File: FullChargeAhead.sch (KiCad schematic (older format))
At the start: 18 parts, among them CON101 USB-MICRO-B, P101 CONN_01X02, P102 JST 2 Pin, U101 MCP73834-FCI/UN

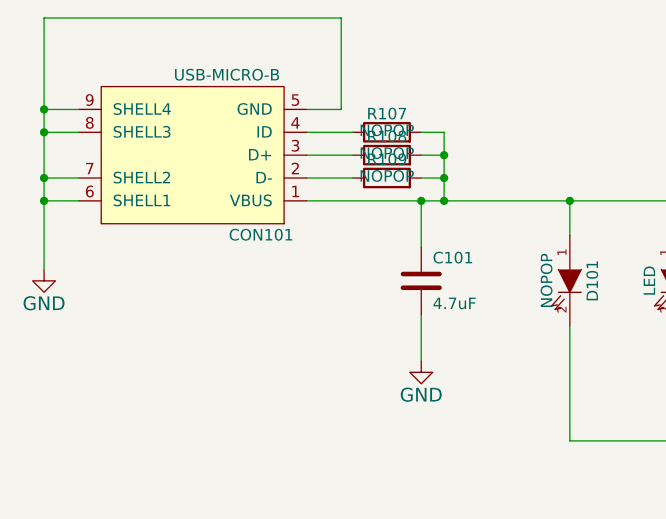
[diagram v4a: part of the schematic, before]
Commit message: Front Cu Layout done
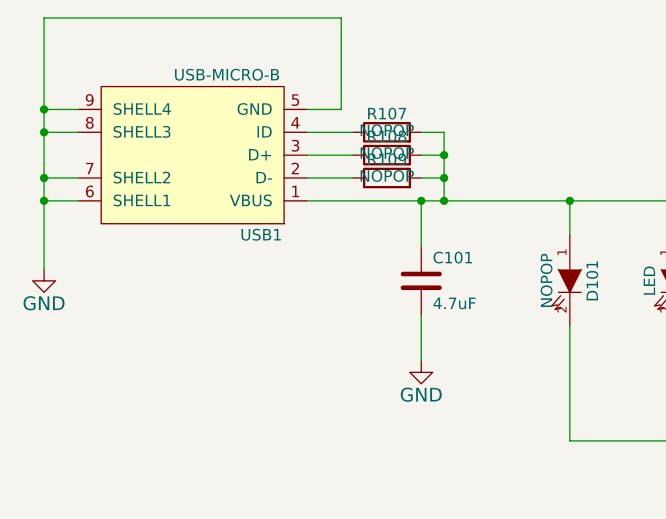
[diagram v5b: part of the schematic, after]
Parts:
- USB1: renamed from CON101; MPN (none) -> Value
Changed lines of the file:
@@
 	5500 4900 5500 5200
 $Comp
-L USB-MICRO-B CON101
+L USB-MICRO-B USB1
 U 1 1 550DCE37
 P 2700 2700
-F 0 "CON101" H 2400 3050 50  0000 C CNN
+F 0 "USB1" H 2400 3050 50  0000 C CNN
 F 1 "USB-MICRO-B" H 2550 2350 50  0000 C CNN
 F 2 "fca-lib:USB_Micro_B" H 2700 2600 50  0001 C CNN
 F 3 "" H 2700 2600 50  0000 C CNN
+F 4 "Value" H 2700 2700 60  0001 C CNN "MPN"
 	1    2700 2700
 	-1   0    0    1

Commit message: Started BOM
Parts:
- C101: ConradPN (none) -> 1278977 - 62
- C102: ConradPN (none) -> 1278977 - 62; MPN (none) -> Value
- D101: ConradPN (none) -> N/A; MPN (none) -> N/A
- D102, D103: ConradPN (none) -> 180102 - 62; MPN (none) -> KP-2012EC
- U101: ConradPN (none) -> 1085505 - 62; MPN (none) -> MCP73834-FCI/UN
- USB1: ConradPN (none) -> N/A; MPN Value -> 10118193-0001LF
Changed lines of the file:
@@
 F 2 "Housings_SSOP:MSOP-10_3x3mm_Pitch0.5mm" H 6700 3350 60  0001 C CNN
 F 3 "" H 6700 3350 60  0000 C CNN
+F 4 "MCP73834-FCI/UN" H 6900 3350 60  0001 C CNN "MPN"
+F 5 "1085505 - 62 " H 6900 3350 60  0001 C CNN "ConradPN"
 	1    6900 3350
 	1    0    0    -1
@@
 F 2 "LEDs:LED-0805" H 4350 3250 60  0001 C CNN
 F 3 "" H 4350 3250 60  0000 C CNN
+F 4 "N/A" H 4350 3250 60  0001 C CNN "MPN"
+F 5 "N/A" H 4350 3250 60  0001 C CNN "ConradPN"
 	1    4350 3250
 	0    1    1    0
@@
 F 2 "LEDs:LED-0805" H 4800 3250 60  0001 C CNN
 F 3 "" H 4800 3250 60  0000 C CNN
+F 4 "KP-2012EC" H 4800 3250 60  0001 C CNN "MPN"
+F 5 "180102 - 62" H 4800 3250 60  0001 C CNN "ConradPN"
 	1    4800 3250
 	0    1    1    0
@@
 F 2 "LEDs:LED-0805" H 5200 3250 60  0001 C CNN
 F 3 "" H 5200 3250 60  0000 C CNN
+F 4 "KP-2012EC" H 5200 3250 60  0001 C CNN "MPN"
+F 5 "180102 - 62" H 5200 3250 60  0001 C CNN "ConradPN"
 	1    5200 3250
 	0    1    1    0
@@
 F 3 "" H 3700 3250 60  0000 C CNN
 F 4 "Value" H 3700 3250 60  0001 C CNN "MPN"
+F 5 "1278977 - 62" H 3700 3250 60  0001 C CNN "ConradPN"
 	1    3700 3250
 	1    0    0    -1
@@
 F 2 "Capacitors_SMD:C_1206_HandSoldering" H 8938 3100 30  0001 C CNN
 F 3 "" H 8900 3250 60  0000 C CNN
+F 4 "Value" H 8900 3250 60  0001 C CNN "MPN"
+F 5 "1278977 - 62" H 8900 3250 60  0001 C CNN "ConradPN"
 	1    8900 3250
 	1    0    0    -1
@@
 F 2 "fca-lib:USB_Micro_B" H 2700 2600 50  0001 C CNN
 F 3 "" H 2700 2600 50  0000 C CNN
-F 4 "Value" H 2700 2700 60  0001 C CNN "MPN"
+F 4 "10118193-0001LF" H 2700 2700 60  0001 C CNN "MPN"
+F 5 "N/A" H 2700 2700 60  0001 C CNN "ConradPN"
 	1    2700 2700
 	-1   0    0    1

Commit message: Some changes and test results
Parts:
- R106: value 1K -> 2K
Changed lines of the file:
@@
 P 8050 3700
 F 0 "R106" V 8130 3700 50  0000 C CNN
-F 1 "1K" V 8057 3701 50  0000 C CNN
+F 1 "2K" V 8057 3701 50  0000 C CNN
 F 2 "Resistors_SMD:R_0805_HandSoldering" V 7980 3700 30  0001 C CNN
 F 3 "" H 8050 3700 30  0000 C CNN
@@
 U 1 1 55106F74
 P 3550 2700
-F 0 "R108" V 3630 2700 50  0000 C CNN
+F 0 "R108" V 3500 2900 50  0000 C CNN
 F 1 "NOPOP" V 3557 2701 50  0000 C CNN
 F 2 "Resistors_SMD:R_0805_HandSoldering" V 3480 2700 30  0001 C CNN
@@
 U 1 1 55106FB8
 P 3550 2800
-F 0 "R109" V 3630 2800 50  0000 C CNN
+F 0 "R109" V 3500 3000 50  0000 C CNN
 F 1 "NOPOP" V 3557 2801 50  0000 C CNN
 F 2 "Resistors_SMD:R_0805_HandSoldering" V 3480 2800 30  0001 C CNN

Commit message: Updated the documentation
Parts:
- D101, D102, D103: symbol LED -> LED-RESCUE-FullChargeAhead
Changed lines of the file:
@@
 EESchema Schematic File Version 2
+LIBS:FullChargeAhead-rescue
 LIBS:power
 LIBS:device
@@
 LIBS:memory
 LIBS:xilinx
-LIBS:special
 LIBS:microcontrollers
 LIBS:dsp
@@
 $EndComp
 $Comp
-L LED D101
+L LED-RESCUE-FullChargeAhead D101
 U 1 1 550DA792
 P 4350 3250
@@
 $EndComp
 $Comp
-L LED D102
+L LED-RESCUE-FullChargeAhead D102
 U 1 1 550DA80B
 P 4800 3250
@@
 $EndComp
 $Comp
-L LED D103
+L LED-RESCUE-FullChargeAhead D103
 U 1 1 550DA883
 P 5200 3250
